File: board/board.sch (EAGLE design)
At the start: 66 parts, among them Q2 ULN2003AD, Y1 8Mhz

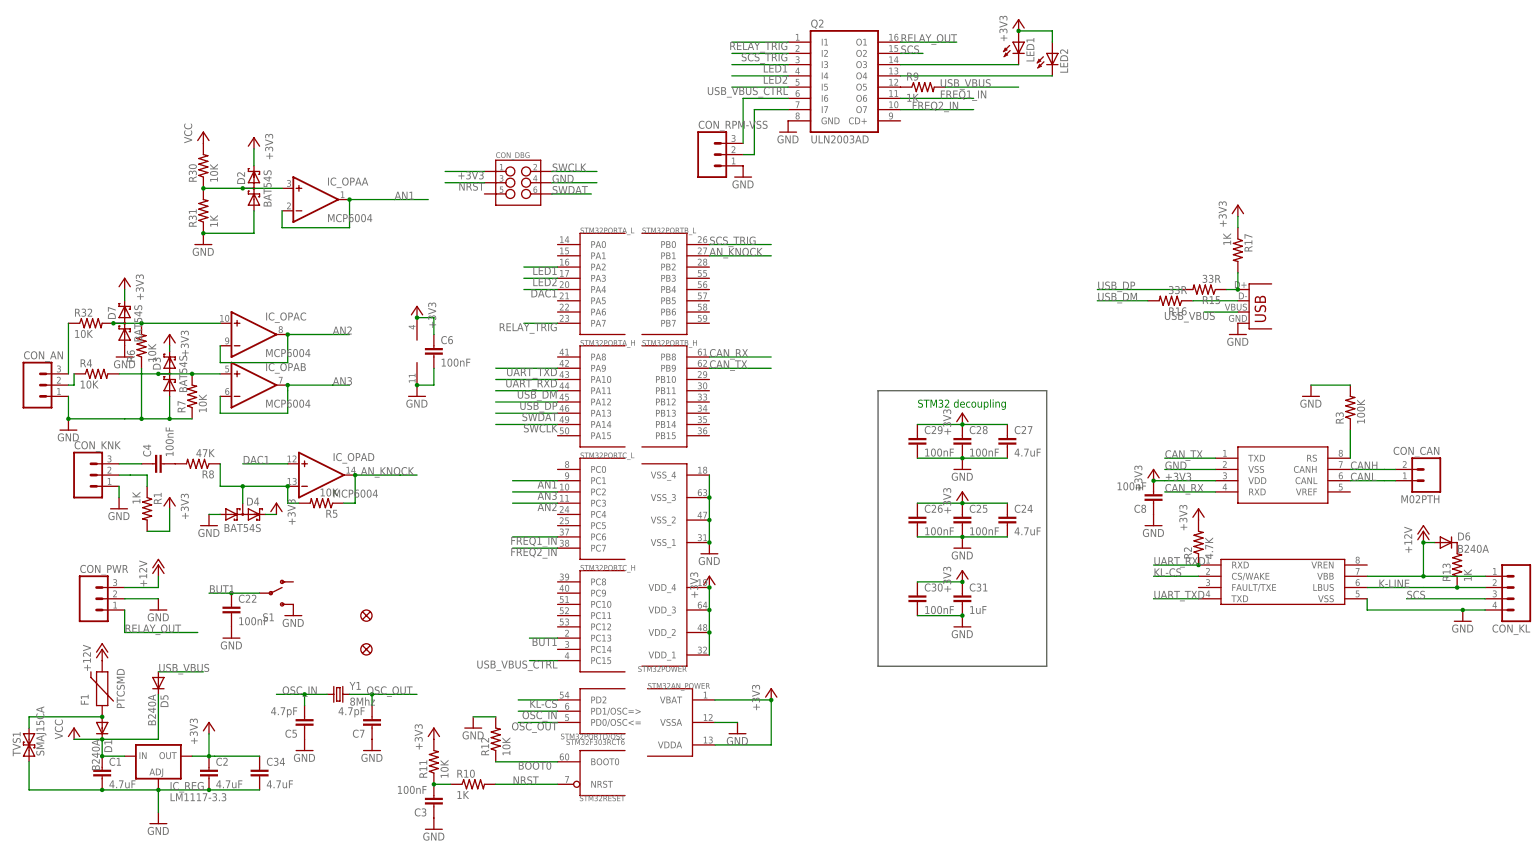
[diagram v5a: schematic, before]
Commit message: [Board] Updated USB with esd/tvs protection, and vbus detection
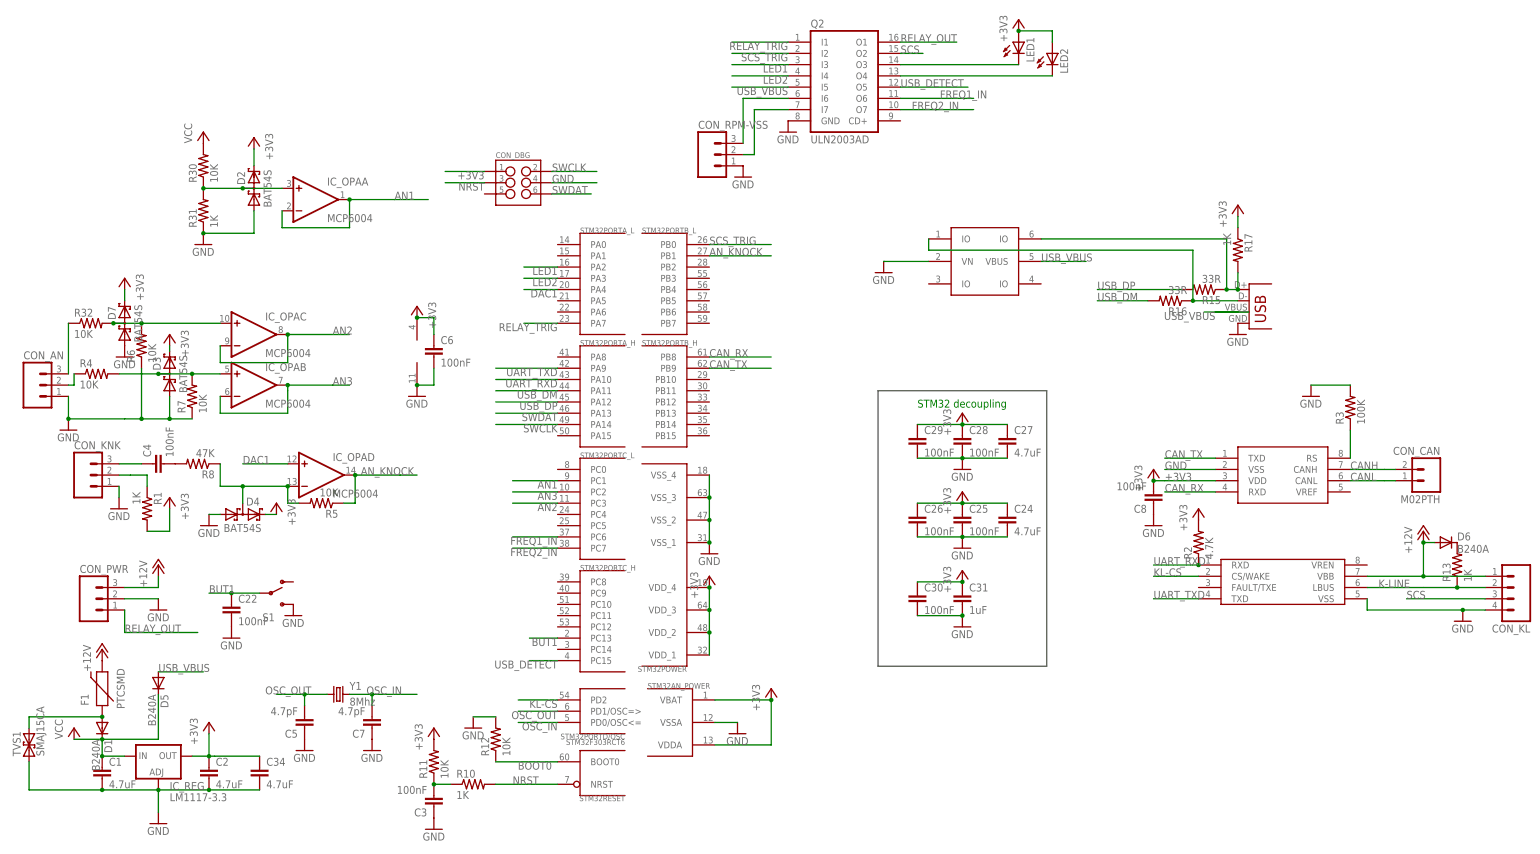
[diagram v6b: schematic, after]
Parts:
- removed FID1, FID2: FIDUCIAL1X2, SparkFun-Aesthetics:FIDUCIAL1X2
- removed R9: 1K, SparkFun-Resistors:RESISTOR0603-RES
- added TVS2: NUP4201MR6, misc:NUP4201MR6
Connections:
- removed net N$7: Q2.O5, R9.1
- removed net USB_VBUS_CTRL: Q2.I5, STM32PORTC_H.PC15
- new net USB_DETECT: Q2.O5, STM32PORTC_H.PC15
- net GND: now also TVS2.VN@2
- net N$17: now also TVS2.IO@6
- net N$19: now also TVS2.IO@1
- net OSC_IN: now also C7.2, STM32PORTD/OSC.PD0/OSC<=, Y1.2; no longer C5.2, STM32PORTD/OSC.PD1/OSC=>, Y1.1
- net OSC_OUT: now also C5.2, STM32PORTD/OSC.PD1/OSC=>, Y1.1; no longer C7.2, STM32PORTD/OSC.PD0/OSC<=, Y1.2
- net USB_VBUS: now also Q2.I5, TVS2.VBUS@5; no longer R9.2
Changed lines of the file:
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@@
 <part name="GND13" library="supply1" deviceset="GND" device=""/>
 <part name="+3V17" library="supply1" deviceset="+3V3" device=""/>
-<part name="R9" library="SparkFun-Resistors" deviceset="RESISTOR" device="0603-RES" value="1K"/>
 <part name="STM32" library="stm32" deviceset="STM32F10XRXT6" device="" value="STM32F303RCT6"/>
 <part name="C3" library="SparkFun-Capacitors" deviceset="CAP" device="0603-CAP" value="100nF"/>
@@
 <part name="CON_KNK" library="SparkFun-Connectors" deviceset="M03" device="PTH"/>
 <part name="+3V3" library="supply1" deviceset="+3V3" device=""/>
-<part name="FID1" library="SparkFun-Aesthetics" deviceset="FIDUCIAL" device="1X2" value="FIDUCIAL1X2"/>
-<part name="FID2" library="SparkFun-Aesthetics" deviceset="FIDUCIAL" device="1X2" value="FIDUCIAL1X2"/>
 <part name="R1" library="SparkFun-Resistors" deviceset="RESISTOR" device="0603-RES" value="1K"/>
 <part name="D5" library="SparkFun-DiscreteSemi" deviceset="DIODE" device="SMA" value="B240A"/>
@@
 <part name="GND12" library="supply1" deviceset="GND" device=""/>
 <part name="GND14" library="supply1" deviceset="GND" device=""/>
+<part name="TVS2" library="misc" deviceset="NUP4201MR6" device=""/>
+<part name="GND18" library="supply1" deviceset="GND" device=""/>
 </parts>
 <sheets>
@@
 <instance part="GND13" gate="1" x="194.31" y="163.83"/>
 <instance part="+3V17" gate="G$1" x="246.38" y="189.23"/>
-<instance part="R9" gate="G$1" x="224.79" y="173.99"/>
 <instance part="STM32" gate="PORTA_L" x="149.86" y="130.81"/>
 <instance part="STM32" gate="PORTA_H" x="149.86" y="102.87"/>
@@
 <instance part="CON_KNK" gate="G$1" x="35.56" y="86.36"/>
 <instance part="+3V3" gate="G$1" x="54.61" y="81.28" rot="MR0"/>
-<instance part="FID1" gate="G$1" x="99.06" y="54.61"/>
-<instance part="FID2" gate="G$1" x="99.06" y="46.99"/>
 <instance part="R1" gate="G$1" x="49.53" y="78.74" rot="R270"/>
 <instance part="D5" gate="G$1" x="52.07" y="39.37" rot="R270"/>
@@
 <instance part="GND12" gate="1" x="100.33" y="24.13"/>
 <instance part="GND14" gate="1" x="85.09" y="24.13"/>
+<instance part="TVS2" gate="G$1" x="238.76" y="134.62"/>
+<instance part="GND18" gate="1" x="215.9" y="132.08"/>
 </instances>
 <busses>
@@
 <wire x1="44.45" y1="58.42" x2="52.07" y2="58.42" width="0.1524" layer="91"/>
 </segment>
+<segment>
+<pinref part="TVS2" gate="G$1" pin="VN@2"/>
+<wire x1="226.06" y1="134.62" x2="215.9" y2="134.62" width="0.1524" layer="91"/>
+<pinref part="GND18" gate="1" pin="GND"/>
+</segment>
 </net>
 <net name="+3V3" class="0">
@@
 <segment>
 <pinref part="JP1" gate="G$1" pin="VBUS"/>
-<wire x1="295.91" y1="123.19" x2="288.29" y2="123.19" width="0.1524" layer="91"/>
+<wire x1="295.91" y1="123.19" x2="290.83" y2="123.19" width="0.1524" layer="91"/>
 <label x="290.83" y="123.19" size="1.778" layer="95" rot="R180"/>
-</segment>
-<segment>
-<wire x1="246.38" y1="173.99" x2="229.87" y2="173.99" width="0.1524" layer="91"/>
-<label x="228.6" y="173.99" size="1.778" layer="95"/>
-<pinref part="R9" gate="G$1" pin="2"/>
+<wire x1="290.83" y1="123.19" x2="288.29" y2="123.19" width="0.1524" layer="91"/>
+<wire x1="298.45" y1="123.19" x2="290.83" y2="123.19" width="0.1524" layer="91"/>
 </segment>
 <segment>
@@
 <wire x1="52.07" y1="41.91" x2="62.23" y2="41.91" width="0.1524" layer="91"/>
 <label x="52.07" y="41.91" size="1.778" layer="95"/>
+</segment>
+<segment>
+<pinref part="TVS2" gate="G$1" pin="VBUS@5"/>
+<wire x1="251.46" y1="134.62" x2="261.62" y2="134.62" width="0.1524" layer="91"/>
+<label x="251.46" y="134.62" size="1.778" layer="95"/>
+</segment>
+<segment>
+<pinref part="Q2" gate="A" pin="I5"/>
+<wire x1="194.31" y1="173.99" x2="181.61" y2="173.99" width="0.1524" layer="91"/>
+<label x="194.31" y="173.99" size="1.778" layer="95" rot="R180"/>
 </segment>
 </net>
@@
 </segment>
 </net>
-<net name="USB_VBUS_CTRL" class="0">
-<segment>
-<wire x1="194.31" y1="173.99" x2="181.61" y2="173.99" width="0.1524" layer="91"/>
-<label x="194.31" y="173.99" size="1.778" layer="95" rot="R180"/>
-<pinref part="Q2" gate="A" pin="I5"/>
-</segment>
-<segment>
-<pinref part="STM32" gate="PORTC_H" pin="PC15"/>
-<wire x1="142.24" y1="44.45" x2="135.89" y2="44.45" width="0.1524" layer="91"/>
-<label x="142.24" y="44.45" size="1.778" layer="95" rot="R180"/>
-</segment>
-</net>
 <net name="N$10" class="0">
 <segment>
@@
 <wire x1="142.24" y1="130.81" x2="134.62" y2="130.81" width="0.1524" layer="91"/>
 <label x="142.24" y="130.81" size="1.778" layer="95" rot="R180"/>
-</segment>
-</net>
-<net name="N$7" class="0">
-<segment>
-<pinref part="Q2" gate="A" pin="O5"/>
-<pinref part="R9" gate="G$1" pin="1"/>
 </segment>
 </net>
@@
 <wire x1="285.75" y1="125.73" x2="295.91" y2="125.73" width="0.1524" layer="91"/>
 <pinref part="R16" gate="G$1" pin="1"/>
+<pinref part="TVS2" gate="G$1" pin="IO@1"/>
+<wire x1="226.06" y1="139.7" x2="226.06" y2="137.16" width="0.1524" layer="91"/>
+<wire x1="226.06" y1="137.16" x2="285.75" y2="137.16" width="0.1524" layer="91"/>
+<wire x1="285.75" y1="137.16" x2="285.75" y2="125.73" width="0.1524" layer="91"/>
+<junction x="285.75" y="125.73"/>
 </segment>
 </net>
@@
 <wire x1="295.91" y1="128.27" x2="295.91" y2="132.08" width="0.1524" layer="91"/>
 <junction x="295.91" y="128.27"/>
+<pinref part="TVS2" gate="G$1" pin="IO@6"/>
+<wire x1="251.46" y1="139.7" x2="293.37" y2="139.7" width="0.1524" layer="91"/>
+<wire x1="293.37" y1="139.7" x2="293.37" y2="128.27" width="0.1524" layer="91"/>
+<junction x="293.37" y="128.27"/>
 </segment>
 </net>
@@
 </segment>
 </net>
-<net name="OSC_IN" class="0">
+<net name="OSC_OUT" class="0">
 <segment>
 <pinref part="STM32" gate="PORTD/OSC" pin="PD1/OSC=&gt;"/>
@@
 <pinref part="Y1" gate="G$1" pin="1"/>
 <wire x1="90.17" y1="36.83" x2="85.09" y2="36.83" width="0.1524" layer="91"/>
-<label x="80.01" y="36.83" size="1.778" layer="95"/>
+<label x="76.2" y="36.83" size="1.778" layer="95"/>
 <pinref part="C5" gate="G$1" pin="2"/>
 <wire x1="85.09" y1="36.83" x2="78.74" y2="36.83" width="0.1524" layer="91"/>
@@
 </segment>
 </net>
-<net name="OSC_OUT" class="0">
+<net name="OSC_IN" class="0">
 <segment>
 <pinref part="STM32" gate="PORTD/OSC" pin="PD0/OSC&lt;="/>
@@
 </segment>
 </net>
+<net name="USB_DETECT" class="0">
+<segment>
+<pinref part="Q2" gate="A" pin="O5"/>
+<wire x1="219.71" y1="173.99" x2="234.95" y2="173.99" width="0.1524" layer="91"/>
+<label x="219.71" y="173.99" size="1.778" layer="95"/>
+</segment>
+<segment>
+<pinref part="STM32" gate="PORTC_H" pin="PC15"/>
+<wire x1="142.24" y1="44.45" x2="135.89" y2="44.45" width="0.1524" layer="91"/>
+<label x="142.24" y="44.45" size="1.778" layer="95" rot="R180"/>
+</segment>
+</net>

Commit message: [Board] Adding/Fixing USB detection and control
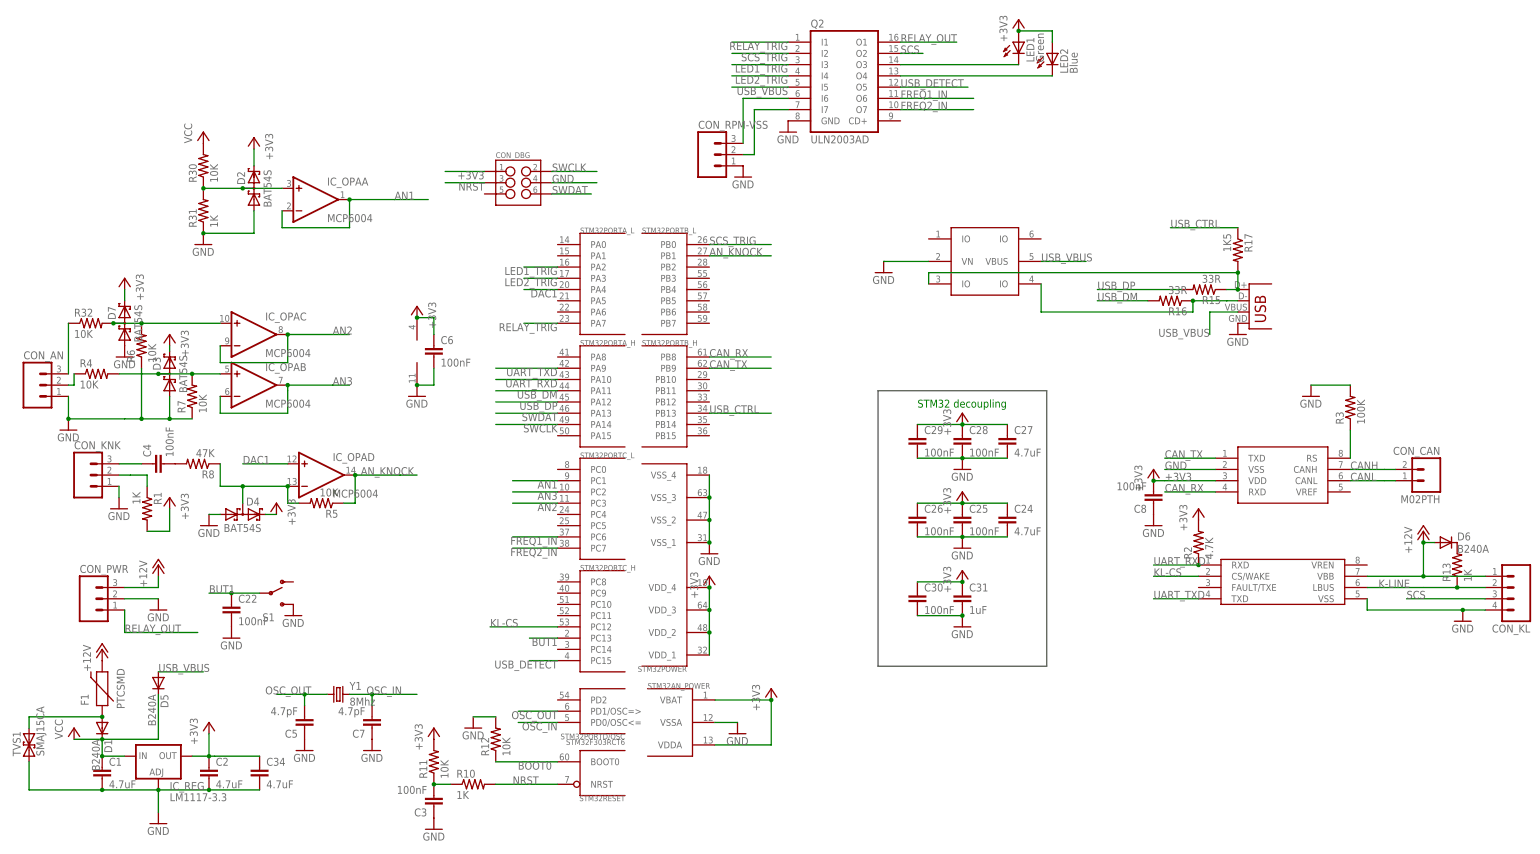
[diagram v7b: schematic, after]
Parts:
- LED1: value (none) -> Green
- LED2: value (none) -> Blue
- R17: value 1K -> 1K5
- renumbered JP1 to CON_USB
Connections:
- net LED1 renamed LED1_TRIG
- net LED2 renamed LED2_TRIG
- removed net N$19: CON_USB.D-, R16.1, TVS2.IO@1
- new net N$7: CON_USB.D+, R15.1, R17.2, TVS2.IO@3
- new net USB_CTRL: R17.1, STM32PORTB_H.PB13
- net +3V3: no longer R17.1
- net KL-CS: now also STM32PORTC_H.PC12; no longer STM32PORTD/OSC.PD2
- net N$17: now also CON_USB.D-, R16.1, TVS2.IO@4; no longer CON_USB.D+, R15.1, R17.2, TVS2.IO@6
